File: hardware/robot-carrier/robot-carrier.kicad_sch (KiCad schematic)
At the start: 36 parts, among them J1 6S BATTERY INPUT, J10 M1 JGA25-2430-CE, J100 PROTECTED 6S BATTERY, J101 EXTERNAL BUCK 5V OUTPUT, J11 M2 JGA25-2430-CE, J12 M3 JGA25-2430-CE, J13 M4 JGA25-2430-CE, J2 BUCK INPUT 24V, J20 SERVO 1, J21 SERVO 2, J22 SERVO 3, J23 SERVO 4, J3 BUCK OUTPUT 5V, J30 WT901 I2C, J40 GA25 L298N LOGIC, J41 GA25 L298N POWER

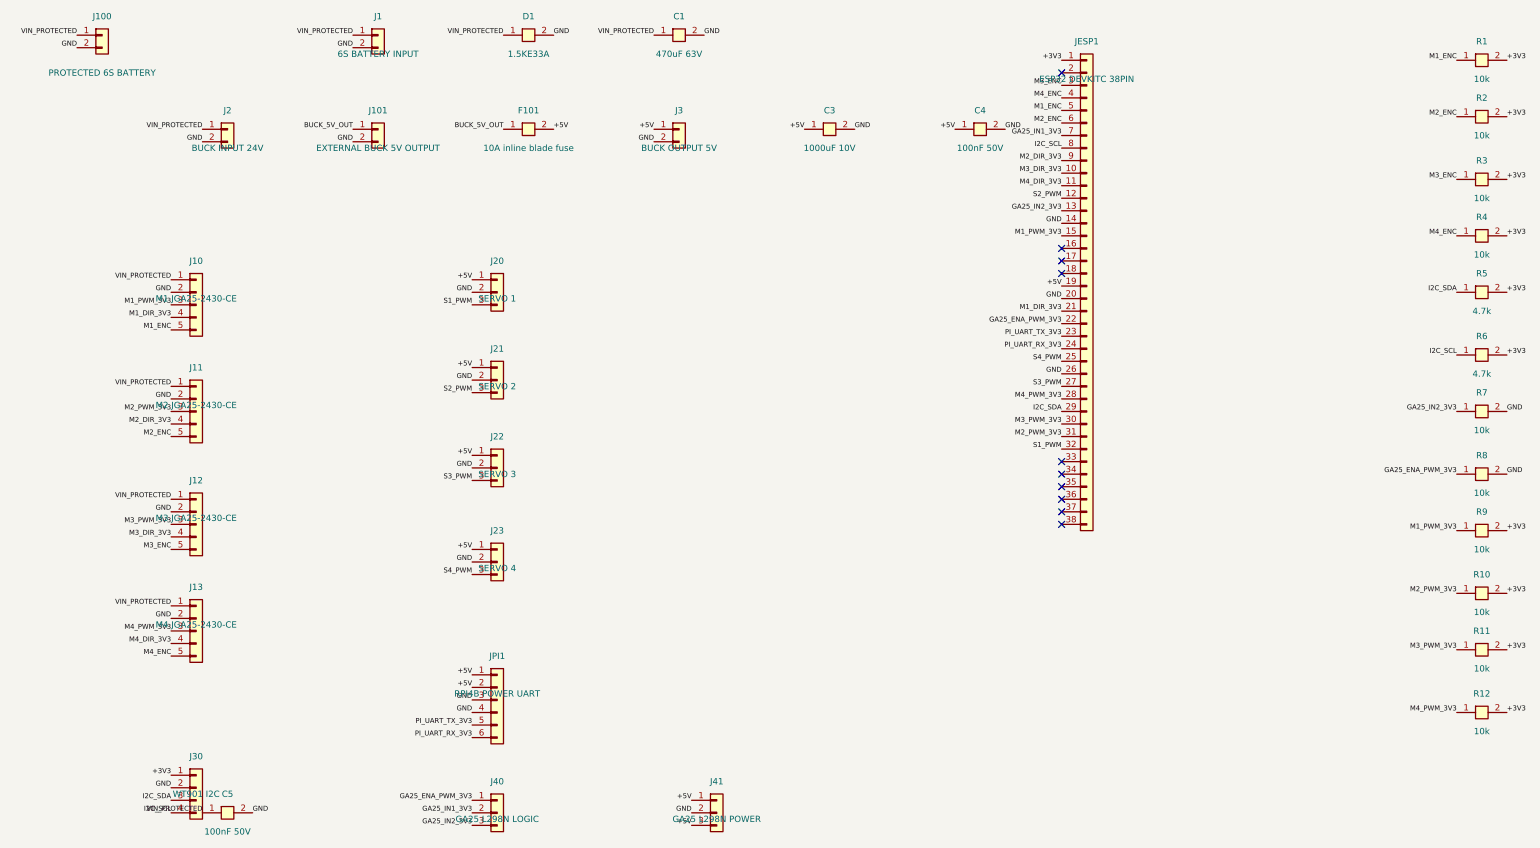
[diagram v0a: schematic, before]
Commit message: Checkpoint autorouted carrier layout
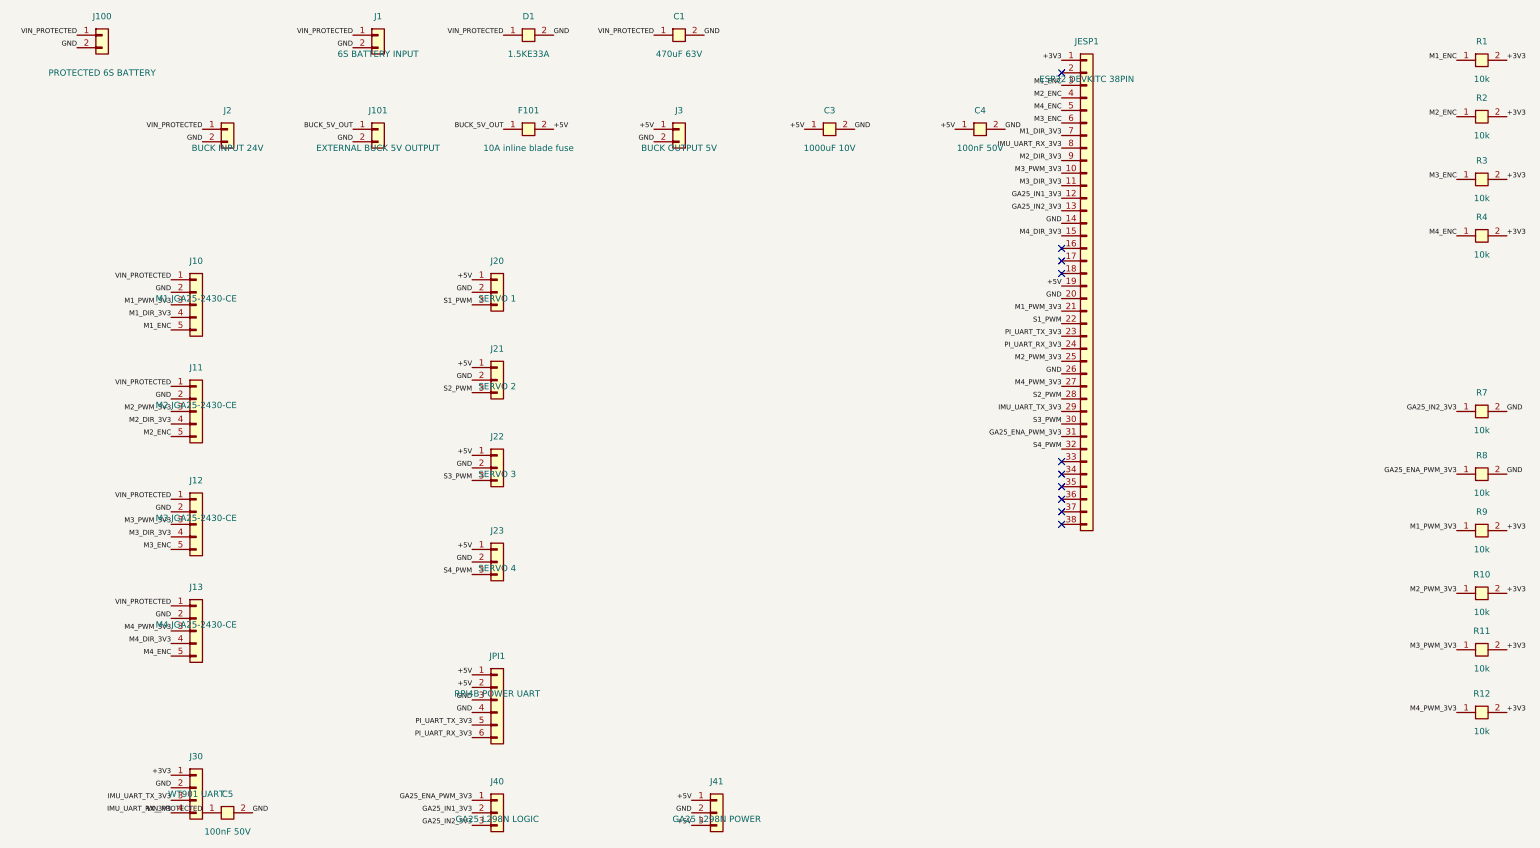
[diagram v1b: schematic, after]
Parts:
- removed R5, R6: 4.7k, Custom:R_1206_HAND, symbol RobotCarrier:R
- J30: value WT901 I2C -> WT901 UART; footprint Custom:I2C_1X04 -> Custom:UART_1X04
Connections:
- net GA25_ENA_PWM_3V3: now also JESP1.31 (Pin_31); no longer JESP1.22 (Pin_22)
- net GA25_IN1_3V3: now also JESP1.12 (Pin_12); no longer JESP1.7 (Pin_7)
- net M1_DIR_3V3: now also JESP1.7 (Pin_7); no longer JESP1.21 (Pin_21)
- net M1_ENC: now also JESP1.3 (Pin_3); no longer JESP1.5 (Pin_5)
- net M1_PWM_3V3: now also JESP1.21 (Pin_21); no longer JESP1.15 (Pin_15)
- net M2_ENC: now also JESP1.4 (Pin_4); no longer JESP1.6 (Pin_6)
- net M2_PWM_3V3: now also JESP1.25 (Pin_25); no longer JESP1.31 (Pin_31)
- net M3_DIR_3V3: now also JESP1.11 (Pin_11); no longer JESP1.10 (Pin_10)
- net M3_ENC: now also JESP1.6 (Pin_6); no longer JESP1.3 (Pin_3)
- net M3_PWM_3V3: now also JESP1.10 (Pin_10); no longer JESP1.30 (Pin_30)
- net M4_DIR_3V3: now also JESP1.15 (Pin_15); no longer JESP1.11 (Pin_11)
- net M4_ENC: now also JESP1.5 (Pin_5); no longer JESP1.4 (Pin_4)
- net M4_PWM_3V3: now also JESP1.27 (Pin_27); no longer JESP1.28 (Pin_28)
- net S1_PWM: now also JESP1.22 (Pin_22); no longer JESP1.32 (Pin_32)
- net S2_PWM: now also JESP1.28 (Pin_28); no longer JESP1.12 (Pin_12)
- net S3_PWM: now also JESP1.30 (Pin_30); no longer JESP1.27 (Pin_27)
- net S4_PWM: now also JESP1.32 (Pin_32); no longer JESP1.25 (Pin_25)
- net I2C_SCL renamed IMU_UART_RX_3V3
- net I2C_SDA renamed IMU_UART_TX_3V3
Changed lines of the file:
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@@
 			)
 		)
-		(property "Value" "WT901 I2C"
+		(property "Value" "WT901 UART"
 			(at 39.37 179.07 0)
 				(effects
@@
 			)
 		)
-		(property "Footprint" "Custom:I2C_1X04"
+		(property "Footprint" "Custom:UART_1X04"
 			(at 39.37 175.26 0)
 				(effects
@@
 			)
 		)
-		(property "Description" "WT901 I2C"
+		(property "Description" "WT901 UART"
 			(at 39.37 175.26 0)
 				(effects
@@
 		)
 	)
-	(label "I2C_SDA"
+	(label "IMU_UART_TX_3V3"
 		(at 34.29 180.34 180)
 			(effects
@@
 		)
 	)
-	(label "I2C_SCL"
+	(label "IMU_UART_RX_3V3"
 		(at 34.29 182.88 180)
 			(effects
@@
 		)
 	)
+	(label "M1_ENC"
+		(at 214.63 35.56 180)
+			(effects
+			(font
+				(size 1 1)
+			)
+			(justify right bottom)
+		)
+	)
+	(label "M2_ENC"
+		(at 214.63 38.1 180)
+			(effects
+			(font
+				(size 1 1)
+			)
+			(justify right bottom)
+		)
+	)
+	(label "M4_ENC"
+		(at 214.63 40.64 180)
+			(effects
+			(font
+				(size 1 1)
+			)
+			(justify right bottom)
+		)
+	)
 	(label "M3_ENC"
-		(at 214.63 35.56 180)
-			(effects
-			(font
-				(size 1 1)
-			)
-			(justify right bottom)
-		)
-	)
-	(label "M4_ENC"
-		(at 214.63 38.1 180)
-			(effects
-			(font
-				(size 1 1)
-			)
-			(justify right bottom)
-		)
-	)
-	(label "M1_ENC"
-		(at 214.63 40.64 180)
-			(effects
-			(font
-				(size 1 1)
-			)
-			(justify right bottom)
-		)
-	)
-	(label "M2_ENC"
 		(at 214.63 43.18 180)
 			(effects
@@
 		)
 	)
-	(label "GA25_IN1_3V3"
+	(label "M1_DIR_3V3"
 		(at 214.63 45.72 180)
 			(effects
@@
 		)
 	)
-	(label "I2C_SCL"
+	(label "IMU_UART_RX_3V3"
 		(at 214.63 48.26 180)
 			(effects
@@
 		)
 	)
+	(label "M3_PWM_3V3"
+		(at 214.63 53.34 180)
+			(effects
+			(font
+				(size 1 1)
+			)
+			(justify right bottom)
+		)
+	)
 	(label "M3_DIR_3V3"
-		(at 214.63 53.34 180)
-			(effects
-			(font
-				(size 1 1)
-			)
-			(justify right bottom)
-		)
-	)
-	(label "M4_DIR_3V3"
 		(at 214.63 55.88 180)
 			(effects
@@
 		)
 	)
-	(label "S2_PWM"
+	(label "GA25_IN1_3V3"
 		(at 214.63 58.42 180)
 			(effects
@@
 		)
 	)
-	(label "M1_PWM_3V3"
+	(label "M4_DIR_3V3"
 		(at 214.63 66.04 180)
 			(effects
@@
 		)
 	)
-	(label "M1_DIR_3V3"
+	(label "M1_PWM_3V3"
 		(at 214.63 81.28 180)
 			(effects
@@
 		)
 	)
-	(label "GA25_ENA_PWM_3V3"
+	(label "S1_PWM"
 		(at 214.63 83.82 180)
 			(effects
@@
 		)
 	)
-	(label "S4_PWM"
+	(label "M2_PWM_3V3"
 		(at 214.63 91.44 180)
 			(effects
@@
 		)
 	)
+	(label "M4_PWM_3V3"
+		(at 214.63 96.52 180)
+			(effects
+			(font
+				(size 1 1)
+			)
+			(justify right bottom)
+		)
+	)
+	(label "S2_PWM"
+		(at 214.63 99.06 180)
+			(effects
+			(font
+				(size 1 1)
+			)
+			(justify right bottom)
+		)
+	)
+	(label "IMU_UART_TX_3V3"
+		(at 214.63 101.6 180)
+			(effects
+			(font
+				(size 1 1)
+			)
+			(justify right bottom)
+		)
+	)
 	(label "S3_PWM"
-		(at 214.63 96.52 180)
-			(effects
-			(font
-				(size 1 1)
-			)
-			(justify right bottom)
-		)
-	)
-	(label "M4_PWM_3V3"
-		(at 214.63 99.06 180)
-			(effects
-			(font
-				(size 1 1)
-			)
-			(justify right bottom)
-		)
-	)
-	(label "I2C_SDA"
-		(at 214.63 101.6 180)
-			(effects
-			(font
-				(size 1 1)
-			)
-			(justify right bottom)
-		)
-	)
-	(label "M3_PWM_3V3"
 		(at 214.63 104.14 180)
 			(effects
@@
 		)
 	)
-	(label "M2_PWM_3V3"
+	(label "GA25_ENA_PWM_3V3"
 		(at 214.63 106.68 180)
 			(effects
@@
 		)
 	)
-	(label "S1_PWM"
+	(label "S4_PWM"
 		(at 214.63 109.22 180)
 			(effects
@@
 			(effects
 			(font
-				(size 1 1)
-			)
-			(justify left bottom)
-		)
-	)
-	(symbol
-		(lib_id "RobotCarrier:R")
-		(at 299.72 77.47 0)
-		(unit 1)
-		(exclude_from_sim no)
-		(in_bom yes)
-		(on_board yes)
-		(dnp no)
-		(property "Reference" "R5"
-			(at 299.72 73.66 0)
-				(effects
-				(font
-					(size 1.27 1.27)
-				)
-			)
-		)
-		(property "Value" "4.7k"
-			(at 299.72 81.28 0)
-				(effects
-				(font
-					(size 1.27 1.27)
-				)
-			)
-		)
-		(property "Footprint" "Custom:R_1206_HAND"
-			(at 299.72 77.47 0)
-				(effects
-				(font
-					(size 1.27 1.27)
-				)
-				(hide yes)
-			)
-		)
-		(property "Datasheet" "~"
-			(at 299.72 77.47 0)
-				(effects
-				(font
-					(size 1.27 1.27)
-				)
-				(hide yes)
-			)
-		)
-		(property "Description" "4.7k"
-			(at 299.72 77.47 0)
-				(effects
-				(font
-					(size 1.27 1.27)
-				)
-				(hide yes)
-			)
-		)
-		(property "LCSC" "C17936"
-			(at 299.72 77.47 0)
-				(effects
-				(font
-					(size 1.27 1.27)
-				)
-				(hide yes)
-			)
-		)
-		(pin "1")
-		(pin "2")
-		(instances
-			(project "robot-carrier"
-				(path "/00000000-0000-4000-8000-000000000001"
-					(reference "R5")
-					(unit 1)
-				)
-			)
-		)
-	)
-	(label "I2C_SDA"
-		(at 294.64 77.47 180)
-			(effects
-			(font
-				(size 1 1)
-			)
-			(justify right bottom)
-		)
-	)
-	(label "+3V3"
-		(at 304.8 77.47 0)
-			(effects
-			(font
-				(size 1 1)
-			)
-			(justify left bottom)
-		)
-	)
-	(symbol
-		(lib_id "RobotCarrier:R")
-		(at 299.72 90.17 0)
-		(unit 1)
-		(exclude_from_sim no)
-		(in_bom yes)
-		(on_board yes)
-		(dnp no)
-		(property "Reference" "R6"
-			(at 299.72 86.36 0)
-				(effects
-				(font
-					(size 1.27 1.27)
-				)
-			)
-		)
-		(property "Value" "4.7k"
-			(at 299.72 93.98 0)
-				(effects
-				(font
-					(size 1.27 1.27)
-				)
-			)
-		)
-		(property "Footprint" "Custom:R_1206_HAND"
-			(at 299.72 90.17 0)
-				(effects
-				(font
-					(size 1.27 1.27)
-				)
-				(hide yes)
-			)
-		)
-		(property "Datasheet" "~"
-			(at 299.72 90.17 0)
-				(effects
-				(font
-					(size 1.27 1.27)
-				)
-				(hide yes)
-			)
-		)
-		(property "Description" "4.7k"
-			(at 299.72 90.17 0)
-				(effects
-				(font
-					(size 1.27 1.27)
-				)
-				(hide yes)
-			)
-		)
-		(property "LCSC" "C17936"
-			(at 299.72 90.17 0)
-				(effects
-				(font
-					(size 1.27 1.27)
-				)
-				(hide yes)
-			)
-		)
-		(pin "1")
-		(pin "2")
-		(instances
-			(project "robot-carrier"
-				(path "/00000000-0000-4000-8000-000000000001"
-					(reference "R6")
-					(unit 1)
-				)
-			)
-		)
-	)
-	(label "I2C_SCL"
-		(at 294.64 90.17 180)
-			(effects
-			(font
-				(size 1 1)
-			)
-			(justify right bottom)
-		)
-	)
-	(label "+3V3"
-		(at 304.8 90.17 0)
-			(effects
-			(font
